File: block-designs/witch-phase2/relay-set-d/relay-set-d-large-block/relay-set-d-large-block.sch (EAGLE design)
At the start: 96 parts, among them IC1 74LVC1G06DBV, IC10 741G3157DBVR, IC11 741G3157DBVR, IC12 74LVC1G79DBV, IC13 74LVC1G79DBV, IC14 74LVC1G79DBV, IC15 74LVC1G79DBV, IC16 74LVC1G79DBV, IC17 74LVC1G08DBV, IC18 74LVC1G08DBV, IC19 74LVC1G08DBV, IC2 74LVC1G06DBV, IC20 74LVC1G08DBV, IC21 74LVC1G08DBV, IC22 74LVC1G08DBV, IC23 74LVC1G08DBV, IC24 74LVC1G08DBV, IC25 74LVC1G08DBV, IC26 74LVC1G08DBV, IC27 741G3157DBVR, IC28 741G3157DBVR, IC29 741G3157DBVR, IC3 74LVC1G06DBV, IC30 741G3157DBVR, IC31 741G3157DBVR, IC32 741G3157DBVR, IC33 741G3157DBVR, IC34 741G3157DBVR, IC35 741G3157DBVR, IC36 741G3157DBVR, IC37 74LVC1G32DBV, IC38 74LVC1G32DBV, IC39 74LVC1G32DBV, IC4 74LVC1G06DBV, IC40 74LVC1G32DBV, IC41 74LVC1G32DBV, IC42 74LVC1G32DBV, IC43 74LVC1G32DBV, IC44 74LVC1G32DBV, IC45 74LVC1G06DBV, IC46 74LVC1G06DBV, IC47 74LVC1G06DBV, IC48 74LVC1G06DBV, IC49 74LVC1G06DBV, IC5 74LVC1G06DBV, IC50 74LVC1G06DBV, IC51 74LVC1G06DBV, IC52 74LVC1G06DBV, IC53 74LVC1G06DBV, IC54 74LVC1G06DBV, IC55 74LVC1G06DBV, IC56 74LVC1G06DBV, IC6 741G3157DBVR, IC7 741G3157DBVR, IC8 741G3157DBVR, IC9 741G3157DBVR, Q1 MMBT2907ALT1SMD, Q2 MMBT2907ALT1SMD

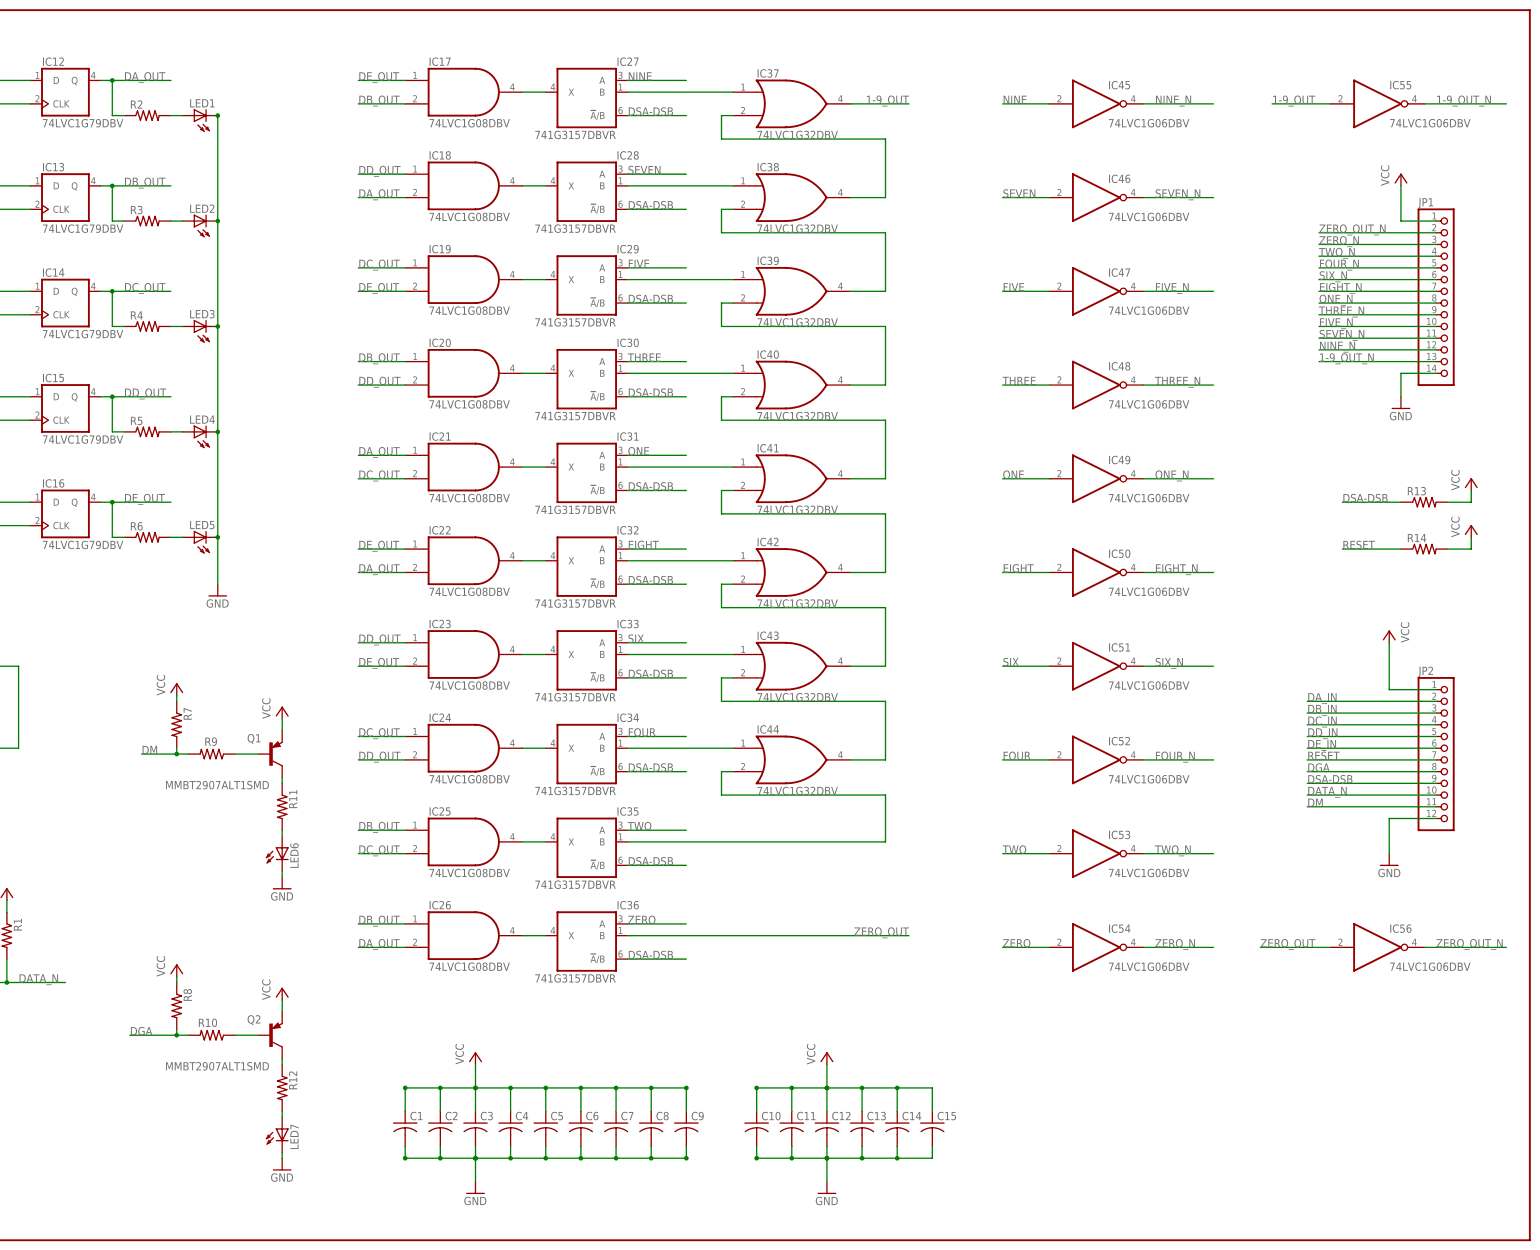
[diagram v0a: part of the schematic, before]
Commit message: add pull down resistors to design
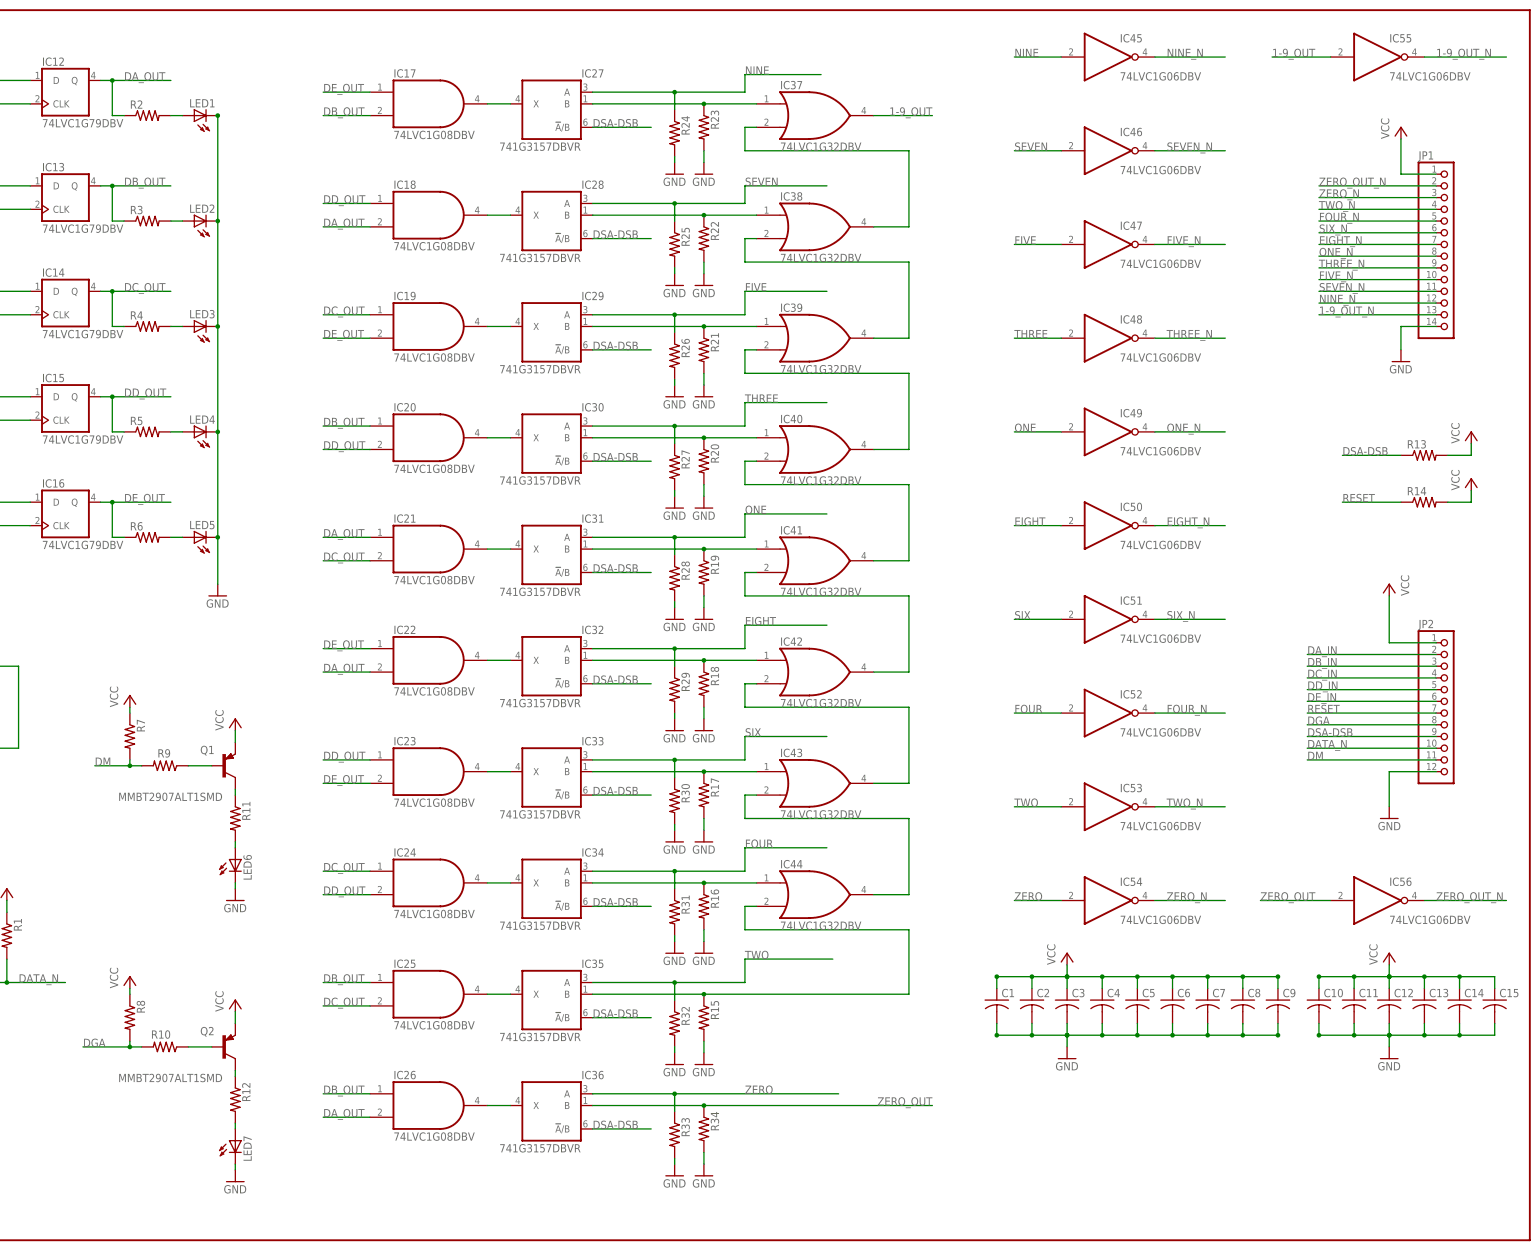
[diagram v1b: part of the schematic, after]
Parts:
- added R15, R16, R17, R18, R19, R20, R21, R22, R23, R24, R25, R26, R27, R28, R29, R30, R31, R32, R33, R34: (no value), resistor:R-US_R0805
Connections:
- net EIGHT: now also R29.1
- net FIVE: now also R26.1
- net FOUR: now also R31.1
- net GND: now also R15.2, R16.2, R17.2, R18.2, R19.2, R20.2, R21.2, R22.2, R23.2, R24.2, R25.2, R26.2, R27.2, R28.2, R29.2, R30.2, R31.2, R32.2, R33.2, R34.2
- net N$10: now also R23.1
- net N$2: now also R15.1
- net N$3: now also R16.1
- net N$4: now also R17.1
- net N$5: now also R18.1
- net N$6: now also R19.1
- net N$7: now also R20.1
- net N$8: now also R21.1
- net N$9: now also R22.1
- net NINE: now also R24.1
- net ONE: now also R28.1
- net SEVEN: now also R25.1
- net SIX: now also R30.1
- net THREE: now also R27.1
- net TWO: now also R32.1
- net ZERO: now also R33.1
- net ZERO_OUT: now also R34.1
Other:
- moved on the sheet: C1, C10, C11, C12, C13, C14, C15, C2, C3, C4, C5, C6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

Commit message: minor tweaks to original large block design
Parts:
- removed IC16: 74LVC1G79DBV, 74xx-little-us:74LVC1G79DBV
- removed R32, R33, R34: (no value), resistor:R-US_R0805
- added C16: (no value), resistor:C-USC0805
- added IC57, IC59: 74LVC1G125DBV, 74xx-little-us:74LVC1G125DBV
- added IC58: 74LVC1G04DBV, 74xx-little-us:74LVC1G04DBV
- IC10, IC28, IC29, IC30, IC31, IC32, IC33, IC34, IC35, IC36, IC6, IC7, IC8, IC9: value 741G3157DBVR -> 74LVC1G125DBV; device 74xx-little-us:741G3157DBVR -> 74xx-little-us:74LVC1G125DBV
- IC11: value 741G3157DBVR -> 741G175; device 74xx-little-us:741G3157DBVR -> 74xx-little-us:741G175
- IC12, IC13, IC14, IC15: value 74LVC1G79DBV -> 741G175; device 74xx-little-us:74LVC1G79DBV -> 74xx-little-us:741G175
- IC27: value 741G3157DBVR -> 74LVC1G04DBV; device 74xx-little-us:741G3157DBVR -> 74xx-little-us:74LVC1G04DBV
- IC45, IC46, IC47, IC48, IC49, IC50, IC51, IC52, IC53, IC54, IC55: value 74LVC1G06DBV -> 74LVC1G04DBV; device 74xx-little-us:74AUC1G06DBV -> 74xx-little-us:74LVC1G04DBV
- IC56: value 74LVC1G06DBV -> 74LVC1G125DBV; device 74xx-little-us:74AUC1G06DBV -> 74xx-little-us:74LVC1G125DBV
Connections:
- removed net LATCH: IC11G$1.X, IC12G$1.D, IC13G$1.D, IC14G$1.D, IC15G$1.D, IC16G$1.D
- removed net N$10: IC27G$1.B, IC37A.I0, R23.1
- removed net N$2: IC35G$1.B, IC44A.I1, R15.1
- removed net N$3: IC34G$1.B, IC44A.I0, R16.1
- removed net N$4: IC33G$1.B, IC43A.I0, R17.1
- removed net N$5: IC32G$1.B, IC42A.I0, R18.1
- removed net N$6: IC31G$1.B, IC41A.I0, R19.1
- removed net N$7: IC30G$1.B, IC40A.I0, R20.1
- removed net N$8: IC29G$1.B, IC39A.I0, R21.1
- removed net N$9: IC28G$1.B, IC38A.I0, R22.1
- removed net ZERO_OUT: IC36G$1.B, IC56G$1.I, R34.1
- new net AB_OUT0: IC56A.I, IC57A.I
- new net DSA-DSB_N: IC57A.OE, IC58A.O, IC59A.OE
- new net OUT0: IC54A.I, IC57A.O, R25.1
- new net OUT1-9: IC55A.I, IC59A.O, R26.1
- net 1-9_OUT: now also IC59A.I; no longer IC55G$1.I
- net 1-9_OUT_N: now also IC55A.O; no longer IC55G$1.O
- net AB_OUT: no longer IC36G$1.X
- net AB_OUT1: now also IC36A.I, IC44A.I1; no longer IC35G$1.X
- net AB_OUT2: now also IC35A.I, IC44A.I0; no longer IC34G$1.X
- net AB_OUT3: now also IC34A.I, IC43A.I0; no longer IC33G$1.X
- net AB_OUT4: now also IC33A.I, IC42A.I0; no longer IC32G$1.X
- net AB_OUT5: now also IC32A.I, IC41A.I0; no longer IC31G$1.X
- net AB_OUT6: now also IC31A.I, IC40A.I0; no longer IC30G$1.X
- net AB_OUT7: now also IC30A.I, IC39A.I0; no longer IC29G$1.X
- net AB_OUT8: now also IC29A.I, IC38A.I0; no longer IC28G$1.X
- net AB_OUT9: now also IC28A.I, IC37A.I0; no longer IC27G$1.X
- net DA: now also IC11G$1.CLK, IC6A.O, R27.1; no longer IC12G$1.CLK, IC6G$1.X
- net DA_IN: now also IC6A.I; no longer IC6G$1.A
- net DA_OUT: now also IC11G$1.Q; no longer IC12G$1.Q
- net DB: now also IC12G$1.CLK, IC7A.O, R28.1; no longer IC13G$1.CLK, IC7G$1.X
- net DB_IN: now also IC7A.I; no longer IC7G$1.A
- net DB_OUT: now also IC12G$1.Q; no longer IC13G$1.Q
- net DC: now also IC13G$1.CLK, IC8A.O, R29.1; no longer IC14G$1.CLK, IC8G$1.X
- net DC_IN: now also IC8A.I; no longer IC8G$1.A
- net DC_OUT: now also IC13G$1.Q; no longer IC14G$1.Q
- net DD: now also IC14G$1.CLK, IC9A.O, R30.1; no longer IC15G$1.CLK, IC9G$1.X
- net DD_IN: now also IC9A.I; no longer IC9G$1.A
- net DD_OUT: now also IC14G$1.Q; no longer IC15G$1.Q
- net DE: now also IC10A.O, IC15G$1.CLK, R31.1; no longer IC10G$1.X, IC16G$1.CLK
- net DE_IN: now also IC10A.I; no longer IC10G$1.A
- net DE_OUT: now also IC15G$1.Q; no longer IC16G$1.Q
- net DGA: now also IC10A.OE, IC6A.OE, IC7A.OE, IC8A.OE, IC9A.OE; no longer IC10G$1.!A!/B, IC11G$1.!A!/B, IC6G$1.!A!/B, IC7G$1.!A!/B, IC8G$1.!A!/B, IC9G$1.!A!/B
- net DSA-DSB: now also IC28A.OE, IC29A.OE, IC30A.OE, IC31A.OE, IC32A.OE, IC33A.OE, IC34A.OE, IC35A.OE, IC36A.OE, IC56A.OE, IC58A.I; no longer IC27G$1.!A!/B, IC28G$1.!A!/B, IC29G$1.!A!/B, IC30G$1.!A!/B, IC31G$1.!A!/B, IC32G$1.!A!/B, IC33G$1.!A!/B, IC34G$1.!A!/B, IC35G$1.!A!/B, IC36G$1.!A!/B
- net EIGHT: now also IC29A.O, IC45A.I, R16.1; no longer IC32G$1.A, IC50G$1.I, R29.1
- net EIGHT_N: now also IC45A.O, JP1.11; no longer IC50G$1.O, JP1.7
- net FIVE: now also IC32A.O, IC48A.I, R19.1; no longer IC29G$1.A, IC47G$1.I, R26.1
- net FIVE_N: now also IC48A.O, JP1.8; no longer IC47G$1.O, JP1.10
- net FOUR: now also IC33A.O, IC49A.I, R20.1; no longer IC34G$1.A, IC52G$1.I, R31.1
- net FOUR_N: now also IC49A.O, JP1.7; no longer IC52G$1.O, JP1.5
- net GND: now also C16.2; no longer IC11G$1.B, R32.2, R33.2, R34.2
- net NINE: now also IC27A.I, IC28A.O, R15.1; no longer IC27G$1.A, IC45G$1.I, R24.1
- net NINE_N: now also IC27A.O; no longer IC45G$1.O
- net ONE: now also IC36A.O, IC52A.I, R23.1; no longer IC31G$1.A, IC49G$1.I, R28.1
- net ONE_N: now also IC52A.O, JP1.4; no longer IC49G$1.O, JP1.8
- net RESET: now also IC11G$1.!CLR, IC12G$1.!CLR, IC13G$1.!CLR, IC14G$1.!CLR, IC15G$1.!CLR; no longer IC10G$1.B, IC6G$1.B, IC7G$1.B, IC8G$1.B, IC9G$1.B
- net SEVEN: now also IC30A.O, IC46A.I, R17.1; no longer IC28G$1.A, IC46G$1.I, R25.1
- net SEVEN_N: now also IC46A.O, JP1.10; no longer IC46G$1.O, JP1.11
- net SIX: now also IC31A.O, IC47A.I, R18.1; no longer IC33G$1.A, IC51G$1.I, R30.1
- net SIX_N: now also IC47A.O, JP1.9; no longer IC51G$1.O, JP1.6
- net THREE: now also IC34A.O, IC50A.I, R21.1; no longer IC30G$1.A, IC48G$1.I, R27.1
- net THREE_N: now also IC50A.O, JP1.6; no longer IC48G$1.O, JP1.9
- net TWO: now also IC35A.O, IC51A.I, R22.1; no longer IC35G$1.A, IC53G$1.I, R32.1
- net TWO_N: now also IC51A.O, JP1.5; no longer IC53G$1.O, JP1.4
- net VCC: now also C16.1, IC11G$1.D, IC12G$1.D, IC13G$1.D, IC14G$1.D, IC15G$1.D; no longer IC11G$1.A
- net ZERO: now also IC53A.I, IC56A.O, R24.1; no longer IC36G$1.A, IC54G$1.I, R33.1
- net ZERO_N: now also IC53A.O; no longer IC54G$1.O
- net ZERO_OUT_N: now also IC54A.O; no longer IC56G$1.O
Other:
- moved on the sheet: C1, C10, C11, C12, C13, C14, C15, C2, C3, C4, C5, C6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
